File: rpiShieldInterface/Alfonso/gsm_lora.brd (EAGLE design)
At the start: 65.3 x 56 mm, 55 parts, among them Q1 MUN2213T1, Q2 MUN2213T1, Q3 MUN2213T1

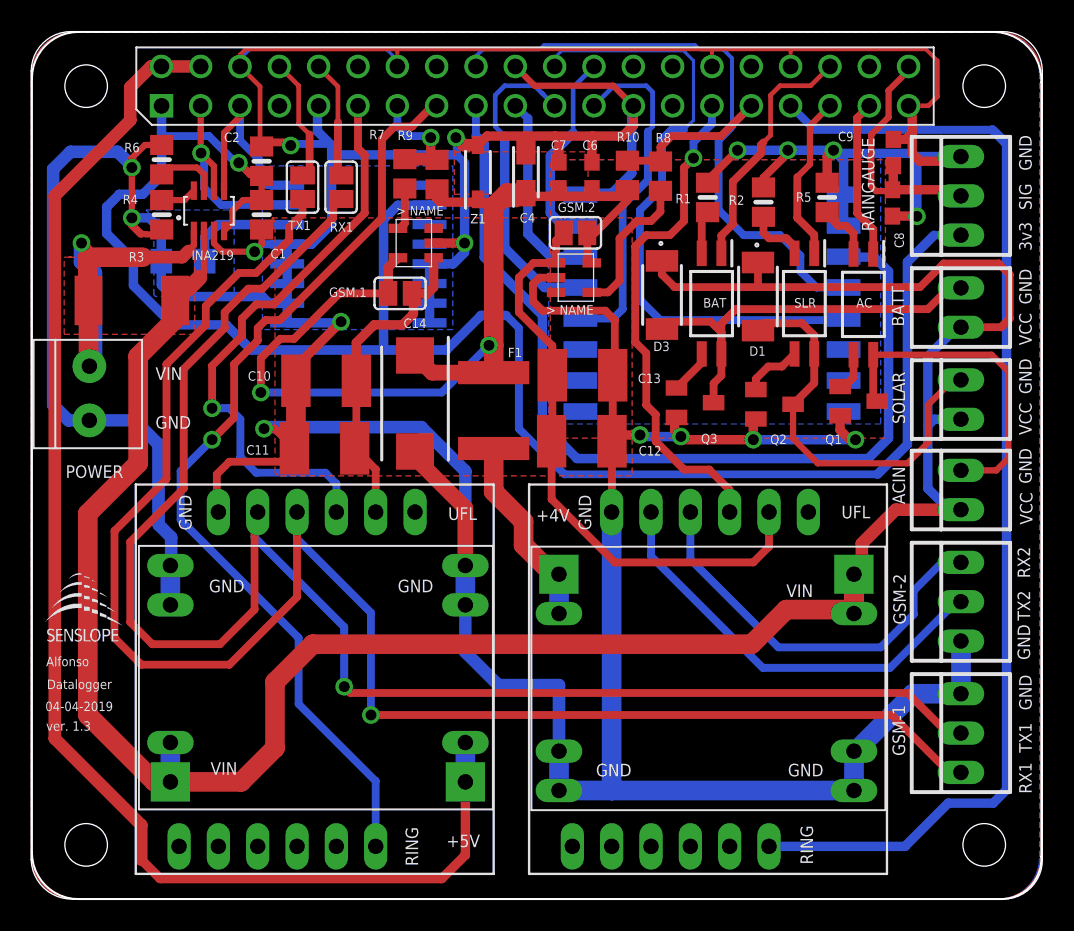
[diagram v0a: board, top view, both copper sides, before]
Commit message: updated schematic and layout for switching function added CAMOutputs
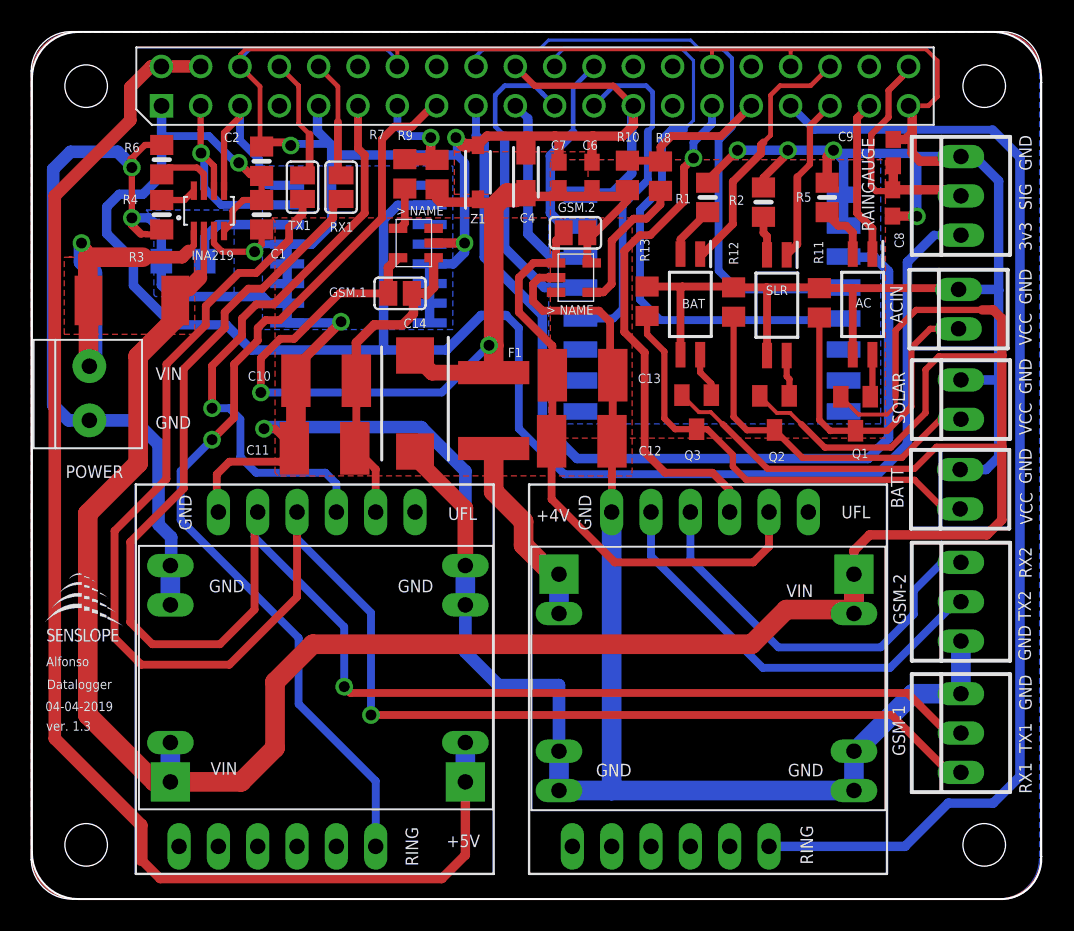
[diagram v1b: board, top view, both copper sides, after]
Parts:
- removed D1, D3: PMEG4010EP,115, PMEG4010EP_115:SOD128
- added R11, R12, R13: 1k, rcl:R0805
- Q1, Q2, Q3: value MUN2213T1 -> (none); device transistor-npn:SC59-BEC -> semicon-smd-ipc:SOT23
- moved BATT 11.7 mm to (60.5, 27.0)
- moved ACIN 11.7 mm to (60.4, 38.6)
- moved SLR 1.78 mm to (48.7, 38.9)
- moved BAT 1.37 mm to (43.1, 38.9)
- moved Q1 0.84 mm to (53.7, 31.9), turned to 180 degrees
- moved Q3 0.62 mm to (43.5, 32.0), turned to 180 degrees
- moved Q2 0.56 mm to (48.5, 31.9), turned to 180 degrees
- moved AC 0.05 mm to (54.2, 38.9)
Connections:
- net +MAIN: now also Q1.2, Q2.2, Q3.2; no longer ACIN.1, BATT.1, D1.1, D3.1, SOLAR.1
- net GND: now also AC.3, ACIN.2, BAT.3, BATT.2, R11.2, R12.2, R13.2, SLR.3, SOLAR.2; no longer Q1.E, Q2.E, Q3.E
- net N$10: now also Q3.1; no longer BATT.2, D3.2, Q3.C
- net N$11: now also Q2.1, SLR.4; no longer Q2.B, SLR.3
- net N$12: now also BATT.1, Q3.3, R13.1; no longer BAT.3, Q3.B
- net N$18: now also Q2.3, R12.1, SOLAR.1; no longer AC.4, ACIN.2, Q1.C
- net N$7: now also AC.4, Q1.1; no longer AC.3, Q1.B
- net N$8: now also ACIN.1, Q1.3, R11.1; no longer D1.2, Q2.C, SLR.4, SOLAR.2
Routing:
- net GND: track 429.6 -> 470.6 mm, vias 16 -> 12
- net +MAIN: track 159.3 -> 186.9 mm
- net N$12: track 2.88 -> 29.0 mm
- net N$10: track 27.5 -> 2.91 mm
- net N$8: track 26.6 -> 20.9 mm
- net RST_LORA: track 38.8 -> 40.8 mm
- net N$18: track 21.3 -> 23.3 mm
- net N$5: track 3.85 -> 2.55 mm
- net N$11: track 3.86 -> 2.69 mm
- net RST2: track 32.7 -> 33.6 mm
- net BATT: track 16.1 -> 16.9 mm
- net RING2: track 73.5 -> 74.2 mm
- net N$9: track 2.82 -> 3.43 mm
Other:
- board size 65.3 x 56 mm -> 65.2 x 56 mm

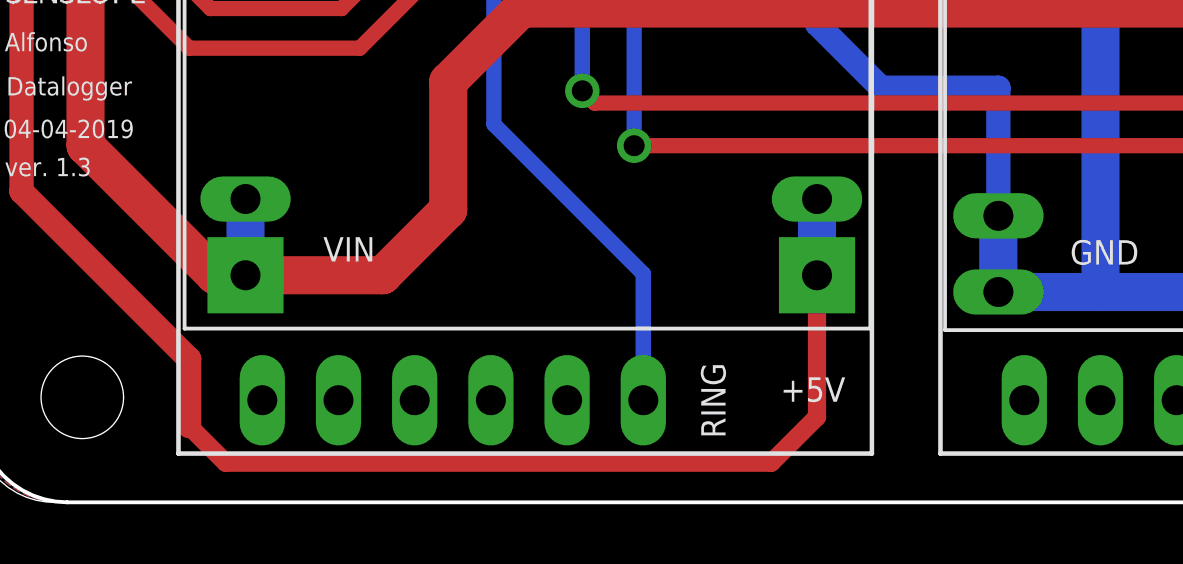
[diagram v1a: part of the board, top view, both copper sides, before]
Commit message: added ptc fuse from 5V out to rpi
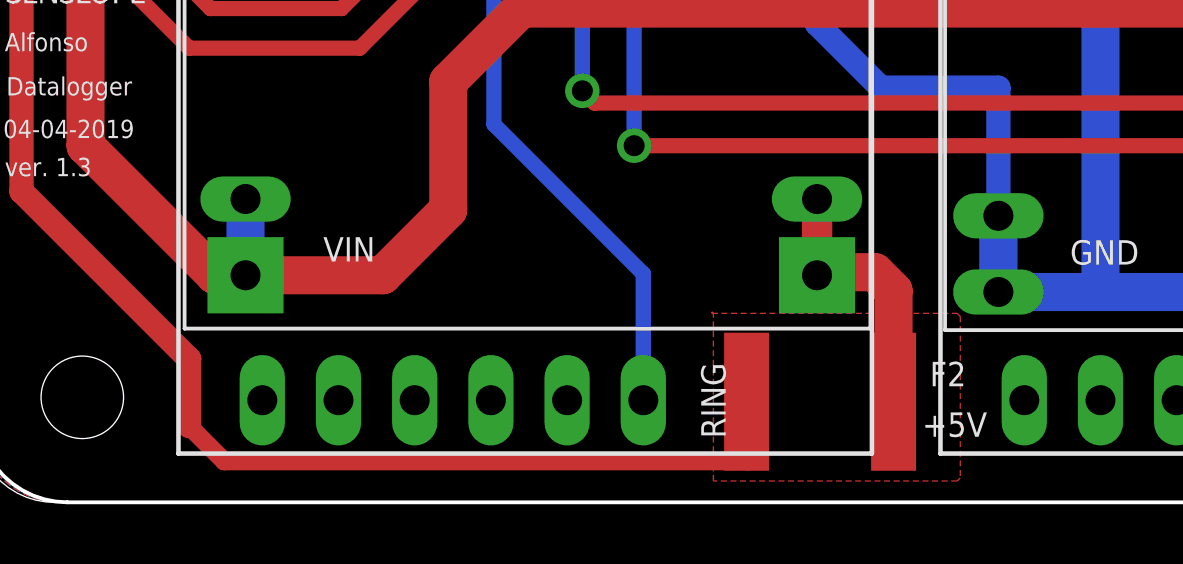
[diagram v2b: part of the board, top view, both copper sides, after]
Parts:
- added F2: MF-SMDF050, fuse:MF-SMDF050
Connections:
- new net N$23: F2.1, U$4.+OUT, U$4.+OUT1
- net 5V_PI: now also F2.2; no longer U$4.+OUT, U$4.+OUT1
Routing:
- net N$23: track 0.00 -> 9.09 mm
- net 5V_PI: track 88.7 -> 80.5 mm
- added copper zone on layer 1, net N$22
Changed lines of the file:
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@@
 <layers>
 <layer number="1" name="Top" color="4" fill="1" visible="yes" active="yes"/>
-<layer number="16" name="Bottom" color="1" fill="1" visible="no" active="yes"/>
+<layer number="16" name="Bottom" color="1" fill="1" visible="yes" active="yes"/>
 <layer number="17" name="Pads" color="2" fill="1" visible="yes" active="yes"/>
 <layer number="18" name="Vias" color="2" fill="1" visible="yes" active="yes"/>
@@
 <text x="10.0584" y="26.6192" size="0.8128" layer="25" ratio="10" rot="R270">GND</text>
 <text x="35.8648" y="26.6192" size="0.8128" layer="25" ratio="10" rot="R270">GND</text>
-<text x="27.3304" y="3.8608" size="0.8128" layer="25" ratio="10">+5V</text>
+<text x="32.0548" y="2.6924" size="0.8128" layer="25" ratio="10">+5V</text>
 <text x="33.1216" y="24.892" size="0.8128" layer="25" ratio="10">+4V</text>
 <text x="52.832" y="25.0952" size="0.8128" layer="25" ratio="10">UFL</text>
@@
 <attribute name="SPICEPREFIX" value="R" x="45.8216" y="39.116" size="1.778" layer="27" rot="R90" display="off"/>
 <attribute name="VALUE" x="48.3616" y="38.481" size="1.27" layer="27" rot="R90"/>
+</element>
+<element name="F2" library="fuse" library_urn="urn:adsk.eagle:library:233" package="MF-SMDF050" package3d_urn="urn:adsk.eagle:package:14081/1" value="MF-SMDF050" x="28.6512" y="3.8608" rot="R180">
+<attribute name="NAME" x="32.3076" y="4.3764" size="0.8128" layer="25" ratio="10"/>
+<attribute name="VALUE" x="39.8518" y="-1.0808" size="1.27" layer="27" rot="R180"/>
 </element>
 </elements>
@@
 <contactref element="U$1" pad="P$2"/>
 <contactref element="U$1" pad="P$4"/>
-<contactref element="U$4" pad="+OUT1"/>
-<contactref element="U$4" pad="+OUT"/>
 <wire x1="2.032" y1="45.9232" x2="2.032" y2="10.8712" width="0.8128" layer="1"/>
 <wire x1="7.62" y1="5.2832" x2="2.032" y2="10.8712" width="0.8128" layer="1"/>
 <wire x1="7.62" y1="5.2832" x2="7.62" y2="3.048" width="0.8128" layer="1"/>
-<wire x1="28.5496" y1="10.6172" x2="28.5496" y2="8.0772" width="1.27" layer="16"/>
 <wire x1="6.9088" y1="50.8" x2="2.032" y2="45.9232" width="0.8128" layer="1"/>
 <wire x1="6.9088" y1="50.8" x2="6.9088" y2="52.9336" width="0.8128" layer="1"/>
@@
 <wire x1="8.255" y1="54.2798" x2="8.9154" y2="54.2798" width="0.8128" layer="1"/>
 <wire x1="8.9154" y1="54.2798" x2="11.4554" y2="54.2798" width="0.8128" layer="1"/>
-<wire x1="7.62" y1="3.048" x2="8.8392" y2="1.8288" width="0.6096" layer="1"/>
-<wire x1="27.0256" y1="1.8288" x2="28.5496" y2="3.3528" width="0.6096" layer="1"/>
-<wire x1="28.5496" y1="3.3528" x2="28.5496" y2="8.0772" width="0.6096" layer="1"/>
-<wire x1="8.8392" y1="1.8288" x2="27.0256" y2="1.8288" width="0.6096" layer="1"/>
+<contactref element="F2" pad="2"/>
+<wire x1="7.62" y1="3.048" x2="8.7884" y2="1.8796" width="0.6096" layer="1"/>
+<wire x1="26.2636" y1="1.8796" x2="26.2012" y2="1.942" width="0.6096" layer="1"/>
+<wire x1="26.2012" y1="1.942" x2="26.2012" y2="3.8608" width="0.6096" layer="1"/>
+<wire x1="8.7884" y1="1.8796" x2="26.2636" y2="1.8796" width="0.6096" layer="1"/>
 </signal>
 <signal name="3V31">
@@
 <wire x1="41.402" y1="31.5468" x2="42.0956" y2="30.8532" width="0.4064" layer="1"/>
 </signal>
+<signal name="N$23">
+<contactref element="U$4" pad="+OUT1"/>
+<contactref element="F2" pad="1"/>
+<contactref element="U$4" pad="+OUT"/>
+<wire x1="28.5496" y1="10.6172" x2="28.5496" y2="8.0772" width="1.016" layer="1"/>
+<wire x1="31.1012" y1="3.8608" x2="31.1012" y2="7.5576" width="1.27" layer="1"/>
+<wire x1="31.1012" y1="7.5576" x2="30.48" y2="8.1788" width="1.27" layer="1"/>
+<wire x1="30.48" y1="8.1788" x2="28.6512" y2="8.1788" width="1.27" layer="1"/>
+<wire x1="28.6512" y1="8.1788" x2="28.5496" y2="8.0772" width="1.27" layer="1"/>
+</signal>
+<signal name="N$22">
+<polygon width="0.1524" layer="1" pour="cutout">
+<vertex x="25.0444" y="6.8072"/>
+<vertex x="33.2232" y="6.8072"/>
+<vertex x="33.3248" y="6.7056"/>
+<vertex x="33.3248" y="1.3208"/>
+<vertex x="33.274" y="1.27"/>
+<vertex x="33.2232" y="1.2192"/>
+<vertex x="25.0952" y="1.2192"/>
+<vertex x="25.0952" y="6.8072"/>
+<vertex x="25.0444" y="6.858"/>
+</polygon>
+</signal>
 </signals>
